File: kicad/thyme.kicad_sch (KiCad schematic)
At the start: 90 parts, among them J1 JST BATTERY R, J2 JST BATTERY R, SW1 SW_Push, SW10 SW_Push, SW11 SW_Push, SW12 SW_Push, SW13 SW_Push, SW14 SW_Push, SW15 SW_Push, SW16 SW_Push, SW17 SW_Push, SW18 SW_Push, SW19 SW_Push, SW2 SW_Push, SW20 SW_Push, SW21 SW_Push, SW22 SW_Push, SW23 SW_Push, SW24 SW_Push, SW25 SW_Push, SW26 SW_Push, SW27 SW_Push, SW28 SW_Push, SW29 SW_Push, SW3 SW_Push, SW30 SW_Push, SW31 SW_Push, SW32 SW_Push, SW33 SW_Push, SW34 SW_Push, SW35 SW_Push, SW36 SW_Push, SW37 SW_Push, SW38 SW_Push, SW39 SW_Push, SW4 SW_Push, SW40 SW_Push, SW41 SW_Push, SW42 SW_Push, SW5 SW_Push, SW6 SW_Push, SW7 SW_Push, SW8 SW_Push, SW9 SW_Push, U1 nice_nano, U2 nice_nano

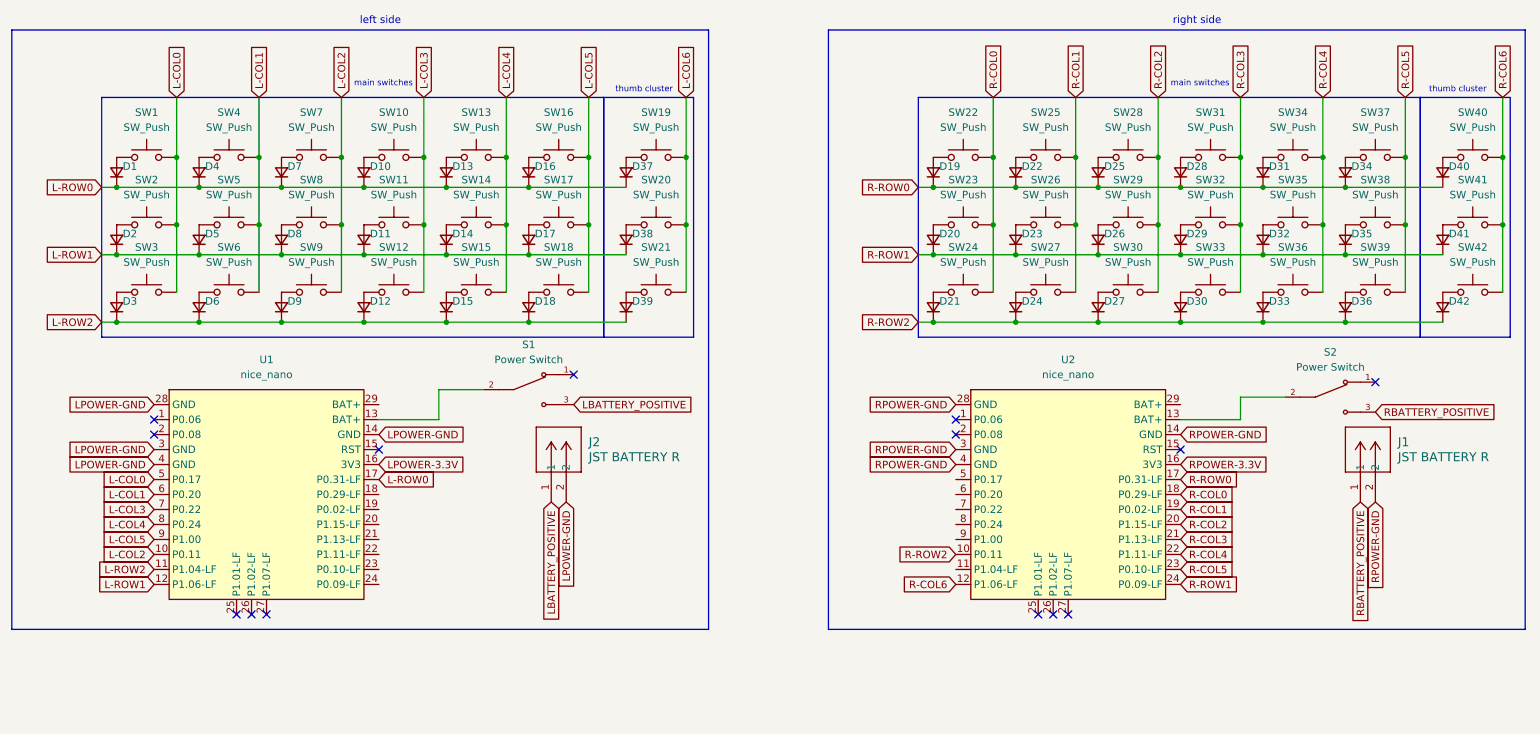
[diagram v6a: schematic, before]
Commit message: feat: use another row instead of col 7
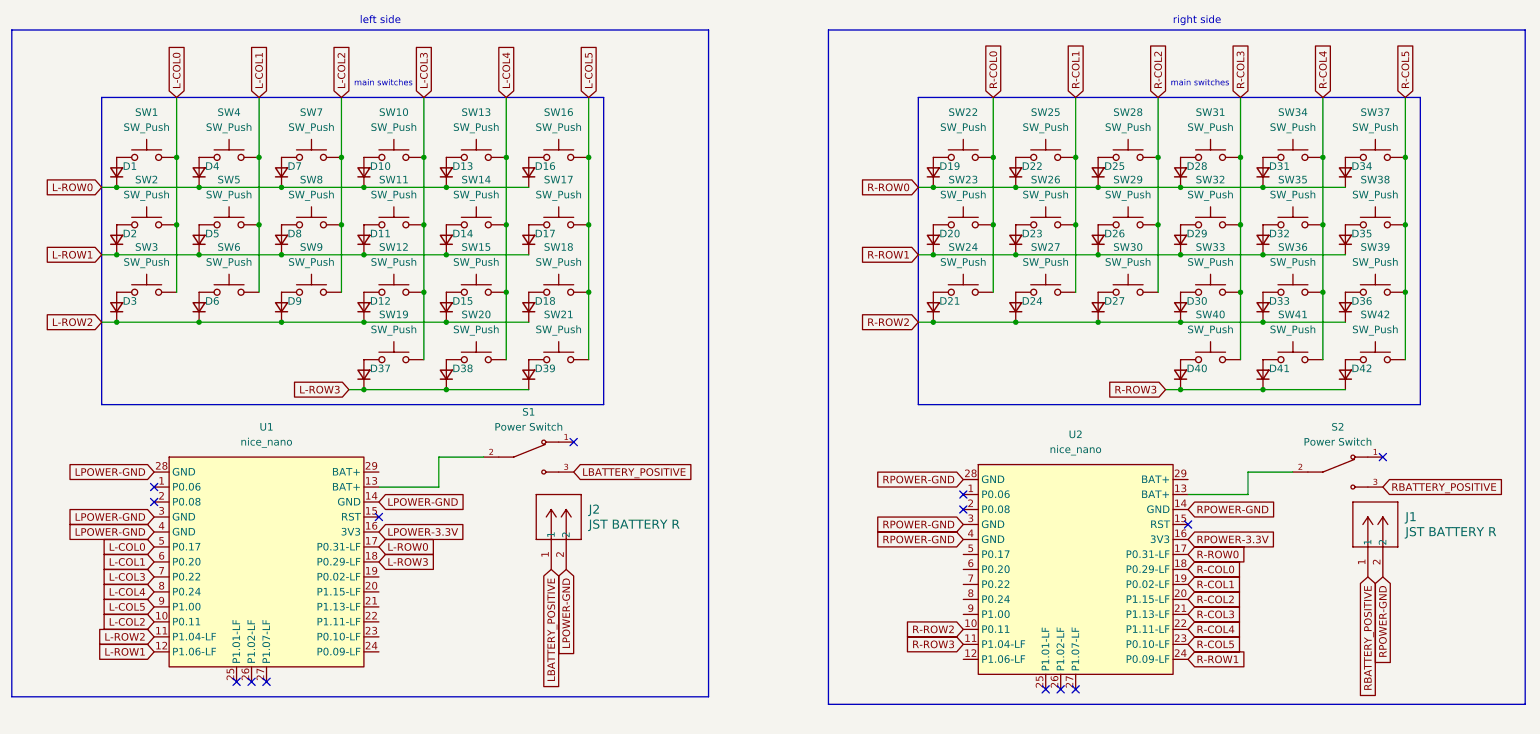
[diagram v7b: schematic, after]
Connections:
- net L-COL3: now also SW19.2
- net L-COL4: now also SW20.2
- net L-COL5: now also SW21.2
- net L-ROW0: no longer D37.1 (K)
- net L-ROW1: no longer D38.1 (K)
- net L-ROW2: no longer D39.1 (K)
- net R-COL3: now also SW40.2
- net R-COL4: now also SW41.2
- net R-COL5: now also SW42.2
- net R-ROW0: no longer D40.1 (K)
- net R-ROW1: no longer D41.1 (K)
- net R-ROW2: no longer D42.1 (K)
- net L-ROW3: now reaches U1.18 (P0.29-LF)
- net L-ROW3: now also D37.1 (K), D38.1 (K), D39.1 (K)
- net R-ROW3: now reaches U2.11 (P1.04-LF)
- net R-ROW3: now also D40.1 (K), D41.1 (K), D42.1 (K)
- removed net L-COL6: SW19.2, SW20.2, SW21.2
- removed net R-COL6: SW40.2, SW41.2, SW42.2, U2.12 (P1.06-LF)
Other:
- note removed: "thumb cluster"
- moved on the sheet: D37, D38, D39, D40, D41, D42, J1, J2, S1, S2, SW19, SW20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

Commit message: feat: redesign edge cuts and key spacing
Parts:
- SW21, SW42: footprint Switch_Keyboard_Kailh:SW_Kailh_Choc_V1V2_1.00u -> Switch_Keyboard_Kailh:SW_Kailh_Choc_V1V2_1.50u
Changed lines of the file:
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@@
 			)
 		)
-		(property "Footprint" "Switch_Keyboard_Kailh:SW_Kailh_Choc_V1V2_1.00u"
+		(property "Footprint" "Switch_Keyboard_Kailh:SW_Kailh_Choc_V1V2_1.50u"
 			(at 113.03 69.85 0)
 			(effects
@@
 			)
 		)
-		(property "Footprint" "Switch_Keyboard_Kailh:SW_Kailh_Choc_V1V2_1.00u"
+		(property "Footprint" "Switch_Keyboard_Kailh:SW_Kailh_Choc_V1V2_1.50u"
 			(at 251.46 69.85 0)
 			(effects
